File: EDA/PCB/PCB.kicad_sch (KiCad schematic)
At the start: 14 parts, among them J1 Conn_01x08_Female, J2 Screw_Terminal_01x02, J3 Screw_Terminal_01x03, J4 Conn_01x02_Male, J5 Conn_01x03_Male, U1 PC817, U2 PC817, U3 WeMos_D1_mini, U4 PC817

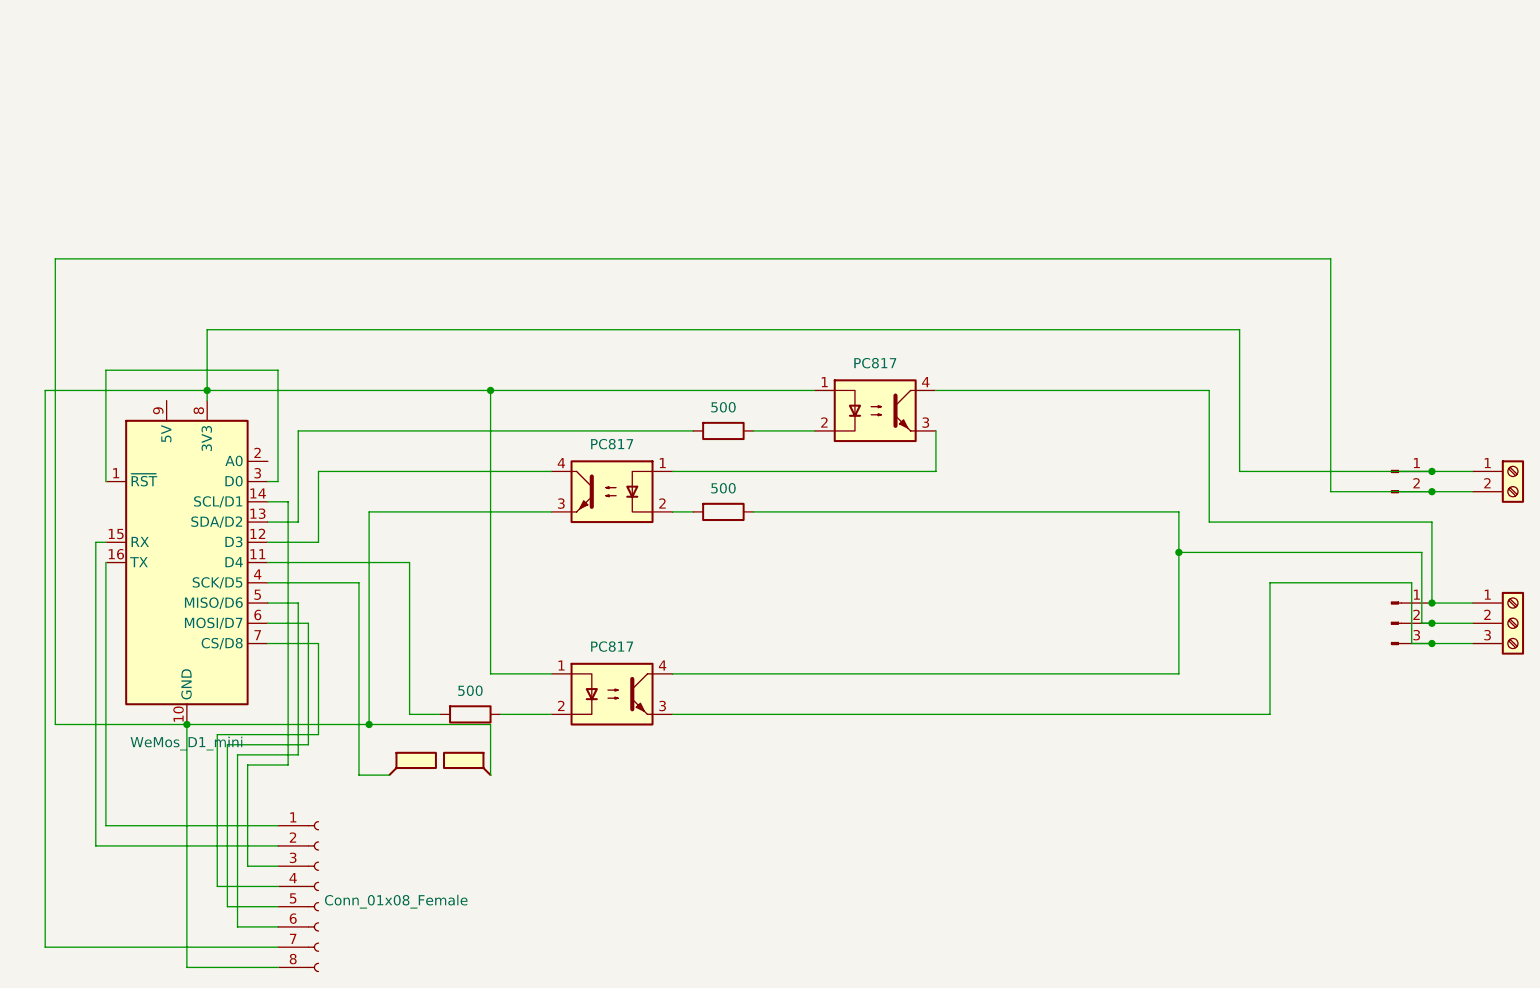
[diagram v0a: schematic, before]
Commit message: Add ground plane
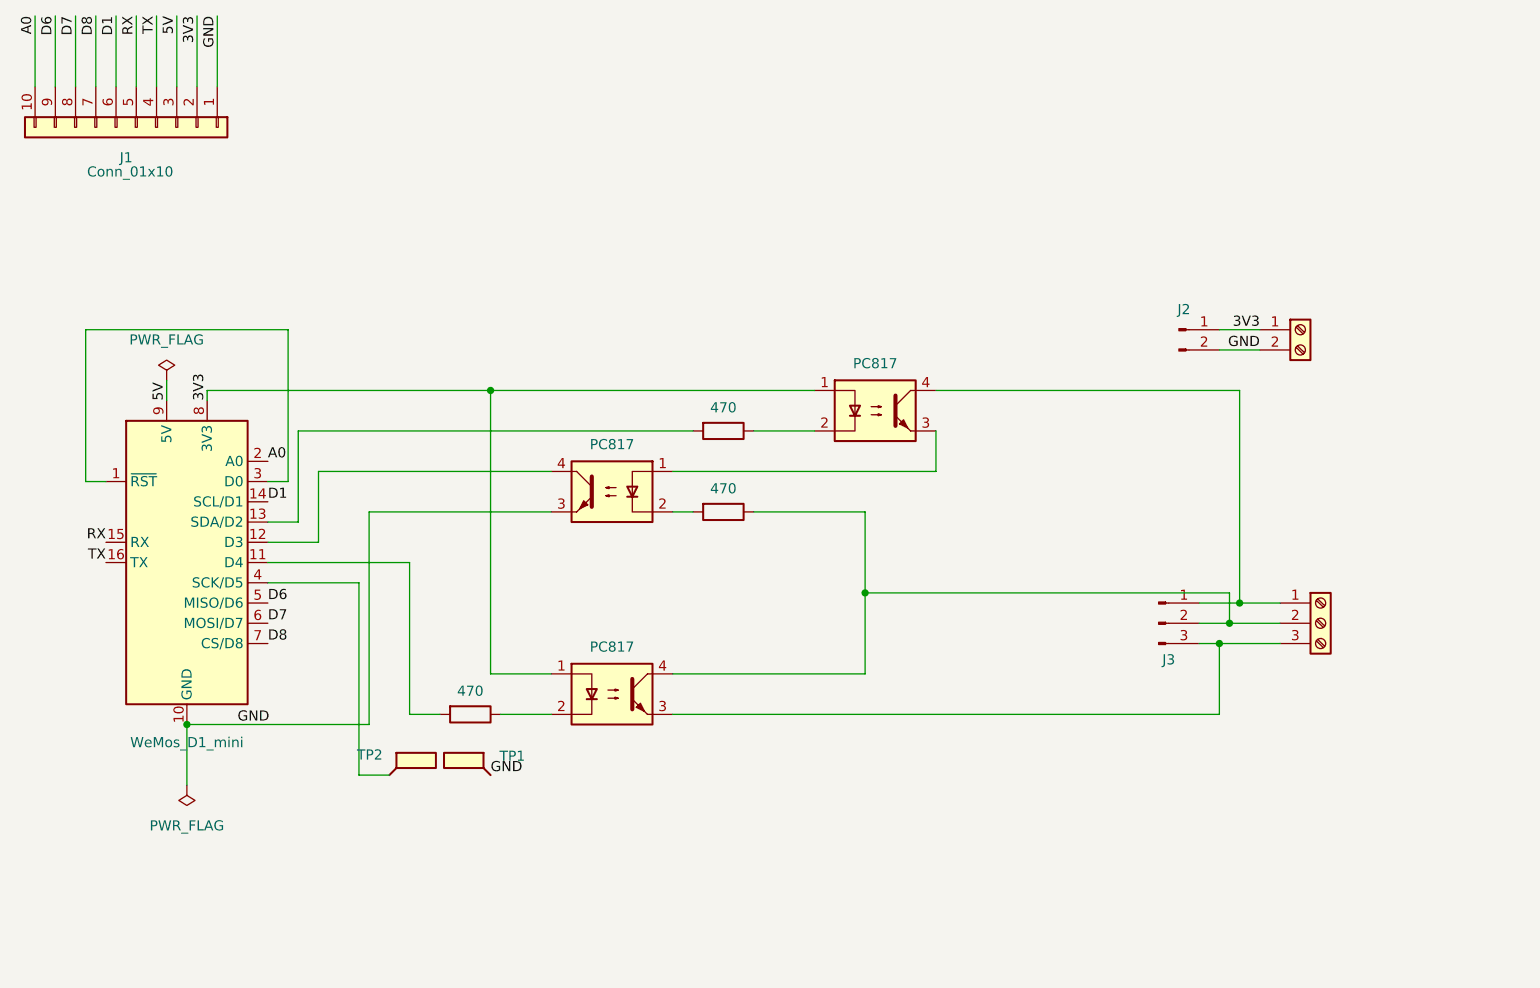
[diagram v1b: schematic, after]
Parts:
- removed J1: Conn_01x08_Female, Connector_PinHeader_2.54mm:PinHeader_1x08_P2.54mm_Vertical, symbol Connector:Conn_01x08_Female
- removed J4: Conn_01x02_Male, Connector_PinHeader_2.54mm:PinHeader_1x02_P2.54mm_Vertical, symbol Connector:Conn_01x02_Male
- removed J5: Conn_01x03_Male, Connector_PinHeader_2.54mm:PinHeader_1x03_P2.54mm_Vertical, symbol Connector:Conn_01x03_Male
- added J1: Conn_01x10, Connector_PinSocket_2.54mm:PinSocket_1x10_P2.54mm_Vertical, symbol Connector_Generic:Conn_01x10
- added J2: Conn_01x02_Pin, Connector_PinSocket_2.54mm:PinSocket_1x02_P2.54mm_Vertical, symbol Connector:Conn_01x02_Pin
- added J3: Conn_01x03_Pin, Connector_PinSocket_2.54mm:PinSocket_1x03_P2.54mm_Vertical, symbol Connector:Conn_01x03_Pin
- R1: renamed from R3; value 500 -> 470
- R2: renamed from R1; value 500 -> 470
- R3: renamed from R2; value 500 -> 470
- renumbered J2 to J4, J3 to J5, TP2 to TP1, TP1 to TP2, U3 to U1, U4 to U3, U1 to U4
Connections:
- net 3V3: now reaches J4.1 (Pin_1), U1.8 (3V3), U3.1, U4.1
- net 3V3: now also J1.2 (Pin_2), J2.1 (Pin_1)
- net at J5.3 (Pin_3), U3.3: now also J3.3 (Pin_3)
- net at J5.2 (Pin_2), R3.1, U3.4: now also J3.2 (Pin_2)
- net GND: now reaches J4.2 (Pin_2), TP1.1, U1.10 (GND), U2.3
- net GND: now also J1.1 (Pin_1), J2.2 (Pin_2)
- net at J5.1 (Pin_1), U4.4: now also J3.1 (Pin_1)
- net D1: now reaches U1.14 (SCL/D1)
- net D1: now also J1.6 (Pin_6)
- net RX: now reaches U1.15 (RX)
- net RX: now also J1.5 (Pin_5)
- net TX: now reaches U1.16 (TX)
- net TX: now also J1.4 (Pin_4)
- net A0: now reaches U1.2 (A0)
- net A0: now also J1.10 (Pin_10)
- net D6: now reaches U1.5 (MISO/D6)
- net D6: now also J1.9 (Pin_9)
- net D7: now reaches U1.6 (MOSI/D7)
- net D7: now also J1.8 (Pin_8)
- net D8: now reaches U1.7 (CS/D8)
- net D8: now also J1.7 (Pin_7)
- net 5V: now reaches U1.9 (5V)
- net 5V: now also J1.3 (Pin_3)

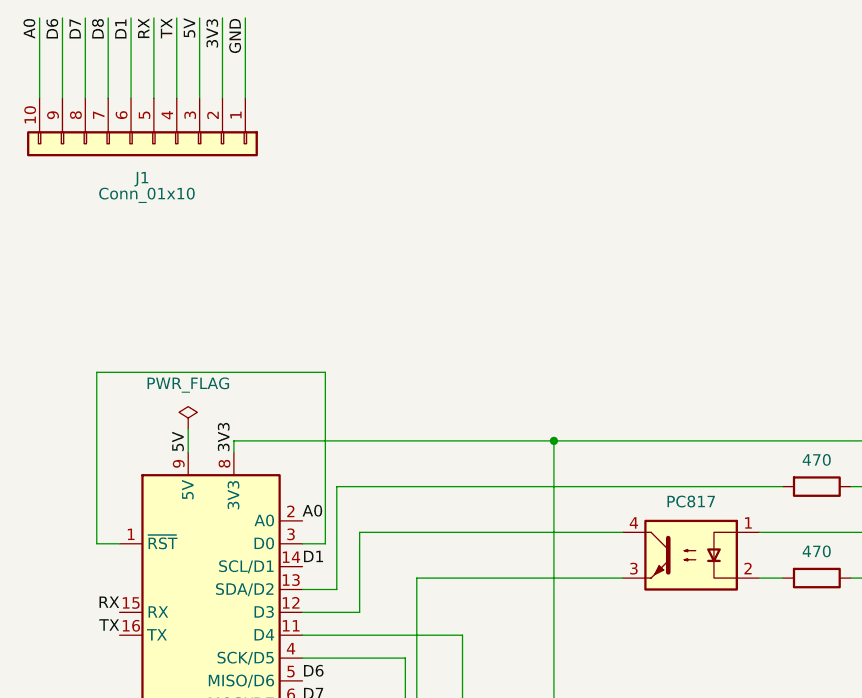
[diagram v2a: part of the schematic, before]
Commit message: Adding the possibilty the use D1 as RX_h
Adding the 10k external pullout
https://github.com/philibertc/micronova_controller/issues/31
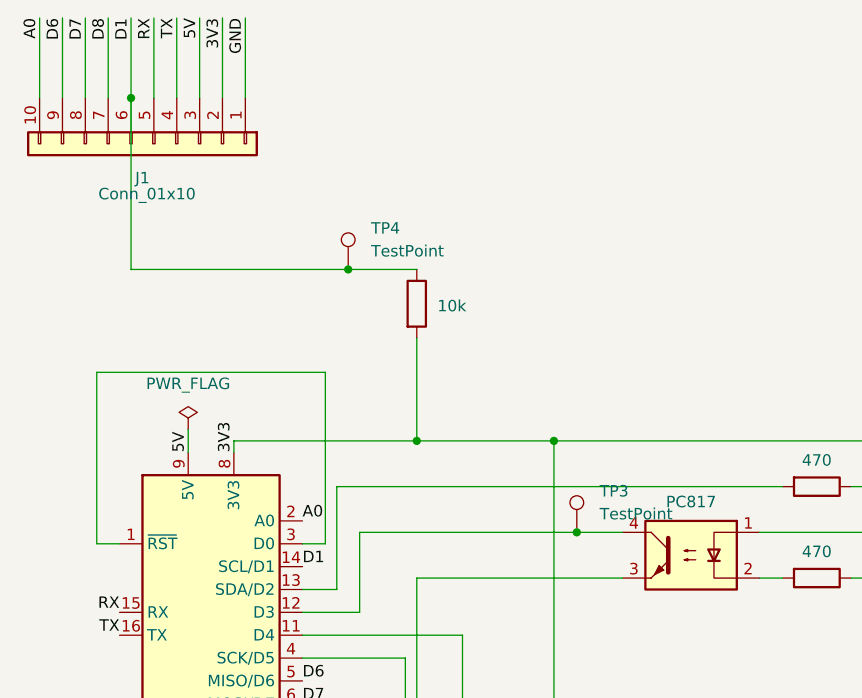
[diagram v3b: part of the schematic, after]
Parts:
- added R4: 10k, Resistor_THT:R_Axial_DIN0207_L6.3mm_D2.5mm_P10.16mm_Horizontal, symbol Device:R
- added TP3, TP4: TestPoint, TestPoint:TestPoint_Pad_1.0x1.0mm, symbol Connector:TestPoint
- U1: footprint Module:WEMOS_D1_mini_light -> RF_Module:WEMOS_D1_mini_light
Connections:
- net 3V3: now also R4.2
- net D1: now also R4.1, TP4.1
- net at U1.12 (D3), U2.4: now also TP3.1
